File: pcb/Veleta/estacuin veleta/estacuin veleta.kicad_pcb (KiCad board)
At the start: 2 copper layers, 39.8 x 50 mm, 19 parts, among them J1 Conn_01x03, J2 Conn_01x03, J3 Conn_01x05, J4 74HC251, J5 Conn_01x09

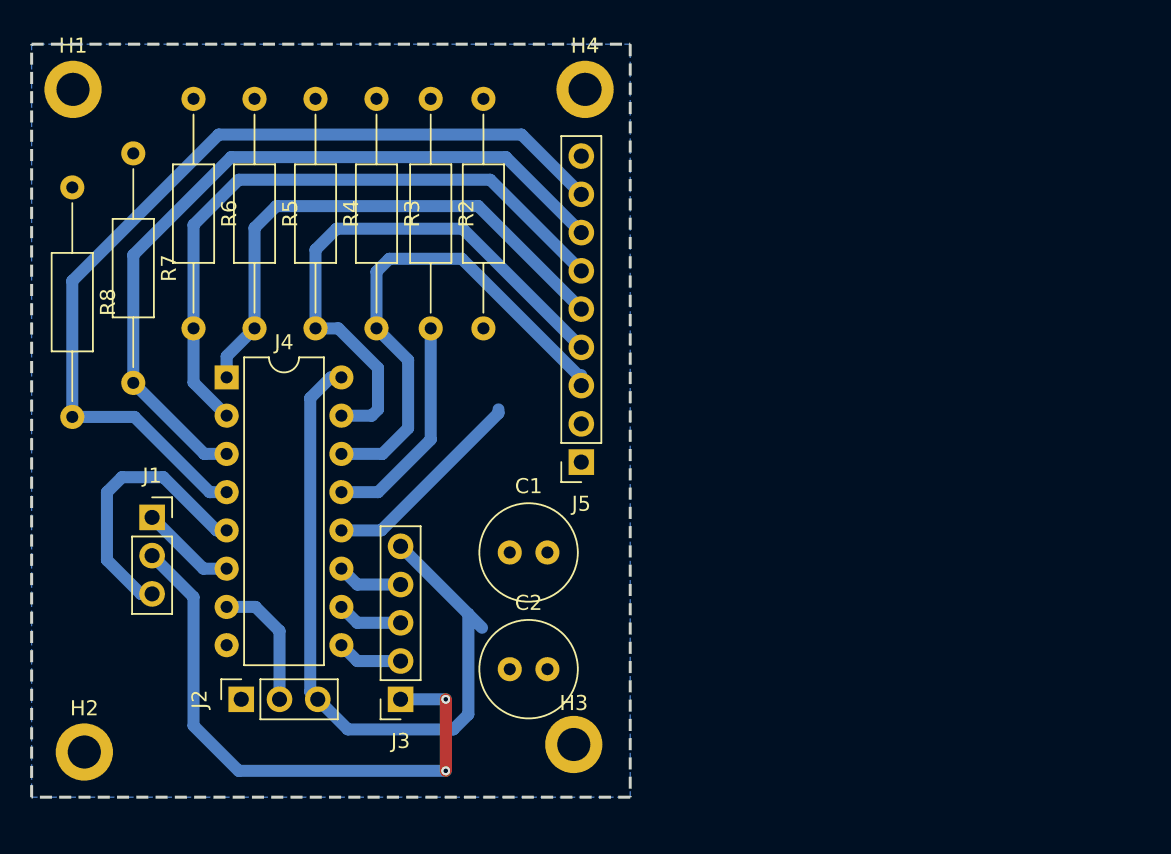
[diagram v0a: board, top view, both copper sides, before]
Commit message: se readaptaron y revisaron las PCBs, listas para imprimir
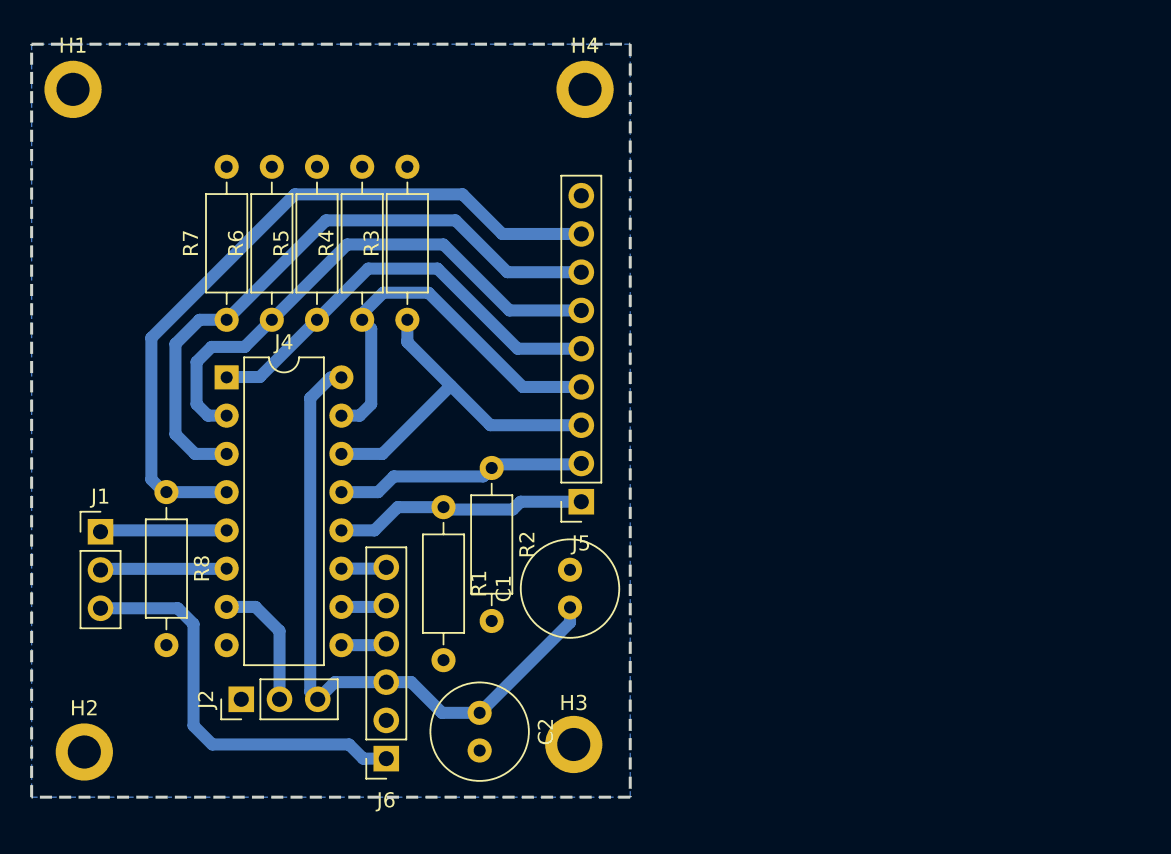
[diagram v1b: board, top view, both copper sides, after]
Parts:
- removed J3: Conn_01x05, Connector_PinSocket_2.54mm:PinSocket_1x05_P2.54mm_Vertical
- added J6: ToMother, Connector_PinSocket_2.54mm:PinSocket_1x06_P2.54mm_Vertical, F.Cu at (108.8, 106.9)
- J1, J2: footprint Connector_PinSocket_2.54mm:PinSocket_1x03_P2.54mm_Vertical -> Connector_PinHeader_2.54mm:PinHeader_1x03_P2.54mm_Vertical
- R1, R2, R3, R4, R5, R6, R7, R8: value R_US -> 10k; footprint Resistor_THT:R_Axial_DIN0207_L6.3mm_D2.5mm_P15.24mm_Horizontal -> Resistor_THT:R_Axial_DIN0207_L6.3mm_D2.5mm_P10.16mm_Horizontal
- moved R1 27.2 mm to (112.6, 90.2)
- moved R2 24.8 mm to (115.8, 87.6)
- moved R8 21.2 mm to (94.2, 89.2)
- moved R6 15.6 mm to (101.2, 77.8), turned to 90 degrees
- moved R5 15.2 mm to (104.2, 77.8), turned to 90 degrees
- moved R4 15.0 mm to (107.2, 77.8), turned to 90 degrees
- moved R3 14.8 mm to (110.2, 77.8), turned to 90 degrees
- moved R7 12.7 mm to (98.2, 77.8), turned to 90 degrees
- moved C1 5.42 mm to (121.0, 96.9), turned to 90 degrees
- moved J1 3.56 mm to (89.8, 91.9)
- moved C2 3.52 mm to (115.0, 103.9), turned to -90 degrees
- moved J5 2.63 mm to (121.8, 89.9)
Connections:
- J4 pad 5: Net-(J1-Pin_3) -> Net-(J1-Pin_1)
- J4 pad 6: Net-(J1-Pin_1) -> Net-(J1-Pin_2)
- R1 pad 1: GND -> Net-(J4-Pin_12)
- R1 pad 2: Net-(J4-Pin_12) -> GND
- R2 pad 1: GND -> Net-(J4-Pin_13)
- R2 pad 2: Net-(J4-Pin_13) -> GND
- R3 pad 1: GND -> Net-(J4-Pin_14)
- R3 pad 2: Net-(J4-Pin_14) -> GND
- R4 pad 1: GND -> Net-(J4-Pin_15)
- R4 pad 2: Net-(J4-Pin_15) -> GND
- R5 pad 1: GND -> Net-(J4-Pin_1)
- R5 pad 2: Net-(J4-Pin_1) -> GND
- R6 pad 1: GND -> Net-(J4-Pin_2)
- R6 pad 2: Net-(J4-Pin_2) -> GND
- R7 pad 1: GND -> Net-(J4-Pin_3)
- R7 pad 2: Net-(J4-Pin_3) -> GND
- R8 pad 1: GND -> Net-(J4-Pin_4)
- R8 pad 2: Net-(J4-Pin_4) -> GND
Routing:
- net Net-(J1-Pin_2): track 38.2 -> 8.41 mm, vias 2 -> 0
- net Net-(J4-Pin_4): track 60.8 -> 48.3 mm
- net Net-(J4-Pin_15): track 37.3 -> 26.3 mm
- net Net-(J4-Pin_14): track 34.4 -> 24.5 mm
- net Net-(J4-Pin_3): track 51.2 -> 41.7 mm
- net Net-(J1-Pin_3): track 18.4 -> 27.1 mm
- net Net-(J4-Pin_2): track 43.1 -> 35.7 mm
- net Net-(J4-Pin_1): track 35.8 -> 28.7 mm
- net +5V: track 48.4 -> 44.4 mm
- net Net-(J4-Pin_12): track 13.9 -> 16.9 mm
- net Net-(J1-Pin_1): track 6.36 -> 8.41 mm
- net Net-(J4-Pin_13): track 14.8 -> 16.7 mm
- net Net-(J4-Pin_10): track 4.37 -> 3.02 mm
- net Net-(J4-Pin_9): track 4.37 -> 3.02 mm
- net Net-(J4-Pin_11): track 4.37 -> 3.02 mm
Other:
- board text removed: "${REFERENCE}"

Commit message: Se agregó la modificación del MQ135 a 5v con divisor resistivo; además de cambio del DHT del pin 12; también se modificaron los pines de conexión
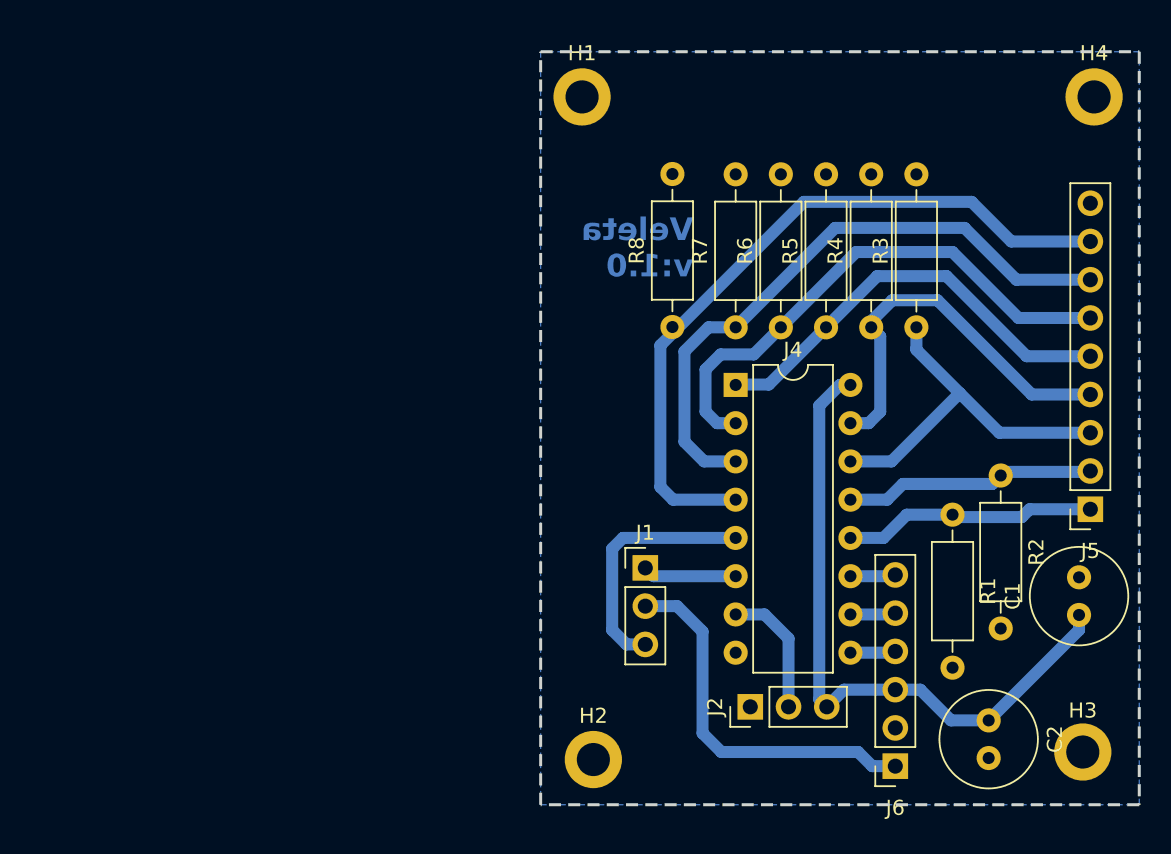
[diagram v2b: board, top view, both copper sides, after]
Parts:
- moved J1 36.3 mm to (126.0, 94.3)
- moved R8 35.3 mm to (127.8, 78.3), turned to 90 degrees
- moved C1 33.8 mm to (154.8, 97.4)
- moved C2 33.8 mm to (148.8, 104.4)
- moved H3 33.8 mm to (155.0, 106.5)
- moved H4 33.8 mm to (155.8, 63.0)
- moved J5 33.8 mm to (155.5, 90.4)
- moved R1 33.8 mm to (146.4, 90.7)
- moved H1 33.8 mm to (121.8, 63.0)
- moved H2 33.8 mm to (122.5, 107.0)
- moved J2 33.8 mm to (133.0, 103.5)
- moved J4 33.8 mm to (132.0, 82.1)
- moved J6 33.8 mm to (142.6, 107.4)
- moved R2 33.8 mm to (149.6, 88.1)
- moved R3 33.8 mm to (144.0, 78.3)
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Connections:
- J4 pad 5: Net-(J1-Pin_1) -> Net-(J1-Pin_3)
- J4 pad 6: Net-(J1-Pin_2) -> Net-(J1-Pin_1)
- J6 pad 1: Net-(J1-Pin_3) -> Net-(J1-Pin_2)
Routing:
- net Net-(J1-Pin_2): track 8.41 -> 25.0 mm
- net Net-(J1-Pin_3): track 27.1 -> 16.5 mm
- net Net-(J1-Pin_1): track 8.41 -> 6.25 mm
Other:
- board text added: "Veleta v:1.0"
